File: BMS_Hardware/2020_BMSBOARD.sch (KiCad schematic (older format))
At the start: 145 parts

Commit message: schematic is done :)
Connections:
- net BUZZER: now also U?.PN2 (D1_8)
- net CELL_1-GND_SENSE: now also U?.PK3 (B2_8)
- net FAN_CTL_1: now also U?.PH2 (D1_3)
- net FAN_CTL_2: now also U?.PH3 (D1_4)
- net FAN_CTL_3: now also U?.PL5 (C1_6)
- net FAN_CTL_4: now also U?.PL4 (C1_5)
- net FAN_PWR: now also U?.PF1 (C1_1)
- net LOGIC_SWITCH: now also U?.PP2 (D1_10)
- net PACK_GATE: now also U?.PN3 (D1_9)
- net PACK_I_SENSE: now also U?.PE0 (B1_3)
- net SER_TX_IND: now also U?.PA5 (B2_10)
- net SW_IND: now also U?.PQ3 (D2_7)
- net TEMP_D_OUT: now also U?.PD1 (D1_6)
- net V_LOG_SENSE: now also U?.PE2 (B1_5)
- net V_OUT_SENSE: now also U?.PE1 (B1_4)
- net CELL8_SENSE: now reaches U?.PD4 (A2_5)
- net CELL7_SENSE: now reaches U?.PD5 (A2_6)
- net CELL6_SENSE: now reaches U?.PB4 (B2_3)
- net CELL5_SENSE: now reaches U?.PB5 (B2_4)
- net CELL4_SENSE: now reaches U?.PK0 (B2_5)
- net CELL3_SENSE: now reaches U?.PK1 (B2_6)
- net CELL2_SENSE: now reaches U?.PK2 (B2_7)
- net SW_EER: now reaches U?.PP3 (D2_8)
- no-connect marks 12 -> 53
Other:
- note added: "A1"
- note added: "A10"
- note added: "A11"
- note added: "A16"
- note added: "A17"
- note added: "A18"
- note added: "A19"
- note added: "A2"
- note added: "A3"
- note added: "A6\n"
- note added: "A7\n"
- moved on the sheet: B?, Conn?, Q?, R?

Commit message: fixed issues
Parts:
- gave numbers to parts that had none: 137
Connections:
- net GND: now also C9.2, D8.2 (A), D9.2 (A), R31.2
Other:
- moved on the sheet: C9, D8, D9, R29, R31

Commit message: schematic finished layout started
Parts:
- B1: footprint (none) -> MRDT_Devices:BUZZER_SMI_1324_TW_5V_2_R
- C1, C10, C11, C12, C13, C14, C15, C16, C17, C18, C19, C2, C20, C21, C3, C4, C5, C6, C7, C8, C9: footprint (none) -> Capacitor_SMD:C_0603_1608Metric_Pad1.05x0.95mm_HandSolder
- Conn1: footprint (none) -> MRDT_Connectors:Anderson_2_Vertical_Sidy_by_Side
- Conn10, Conn11: footprint (none) -> MRDT_Connectors:MOLEX_SL_09_Vertical
- Conn2, Conn5, Conn6, Conn7, Conn8: footprint (none) -> MRDT_Connectors:MOLEX_SL_02_Vertical
- Conn3, SW1: footprint (none) -> MRDT_Connectors:MOLEX_SL_04_Vertical
- Conn4, Conn9: footprint (none) -> MRDT_Connectors:MOLEX_SL_03_Vertical
- D1, D10, D11, D12, D13, D14, D15, D16, D2, D21, D23, D3, D4, D5, D6, D7, D8, D9: footprint (none) -> Diode_SMD:D_SOD-323_HandSoldering
- D17, D18, D19, D20, D22: footprint (none) -> LED_SMD:LED_0603_1608Metric_Pad1.05x0.95mm_HandSolder
- F1: footprint (none) -> Fuse:Fuse_0603_1608Metric_Pad1.05x0.95mm_HandSolder
- Q2, Q3: footprint (none) -> MRDT_Actives:IRLS3034_TO-263-7_P
- R1, R10, R11, R12, R13, R14, R15, R16, R17, R18, R19, R2, R20, R21, R22, R23, R24, R25, R26, R27, R28, R29, R3, R30, R31, R32, R33, R34, R35, R36, R37, R38, R39, R4, R40, R41, R42, R43, R44, R45, R46, R47, R48, R49, R5, R50, R51, R52, R53, R54, R55, R56, R6, R7, R8, R9: footprint (none) -> Resistor_SMD:R_0603_1608Metric_Pad1.05x0.95mm_HandSolder
- U1: footprint (none) -> Package_SO:SOIC-8-1EP_3.9x4.9mm_P1.27mm_EP2.29x3mm
- U10, U12: footprint (none) -> MRDT_Devices:OKI_Horizontal
- U11: footprint (none) -> MRDT_Shields:TM4C129E_Launchpad_FULL_SMD_TOP
- U2, U3, U4, U5, U6, U7, U8: footprint (none) -> Package_SO:SO-8_5.3x6.2mm_P1.27mm
- U9: footprint (none) -> MRDT_Sensors:ACS759ECB_PFF_Leadform_5pins
- V1, V2, V3: footprint (none) -> MRDT_Drill_Holes:BATT_PWR_VIA
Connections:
- net CELL_2_SENSE is gone; now on net CELL2_SENSE: D13.1 (K), R35.1
- net CELL_3_SENSE is gone; now on net CELL3_SENSE: D12.1 (K), R34.1
- net CELL_4_SENSE is gone; now on net CELL4_SENSE: D11.1 (K), R33.1
- net CELL_5_SENSE is gone; now on net CELL5_SENSE: D10.1 (K), R32.1
- net CELL_6_SENSE is gone; now on net CELL6_SENSE: D16.1 (K), R38.1
- net CELL_7_SENSE is gone; now on net CELL7_SENSE: D15.1 (K), R37.1
- net CELL_8_SENSE is gone; now on net CELL8_SENSE: D14.1 (K), R36.1

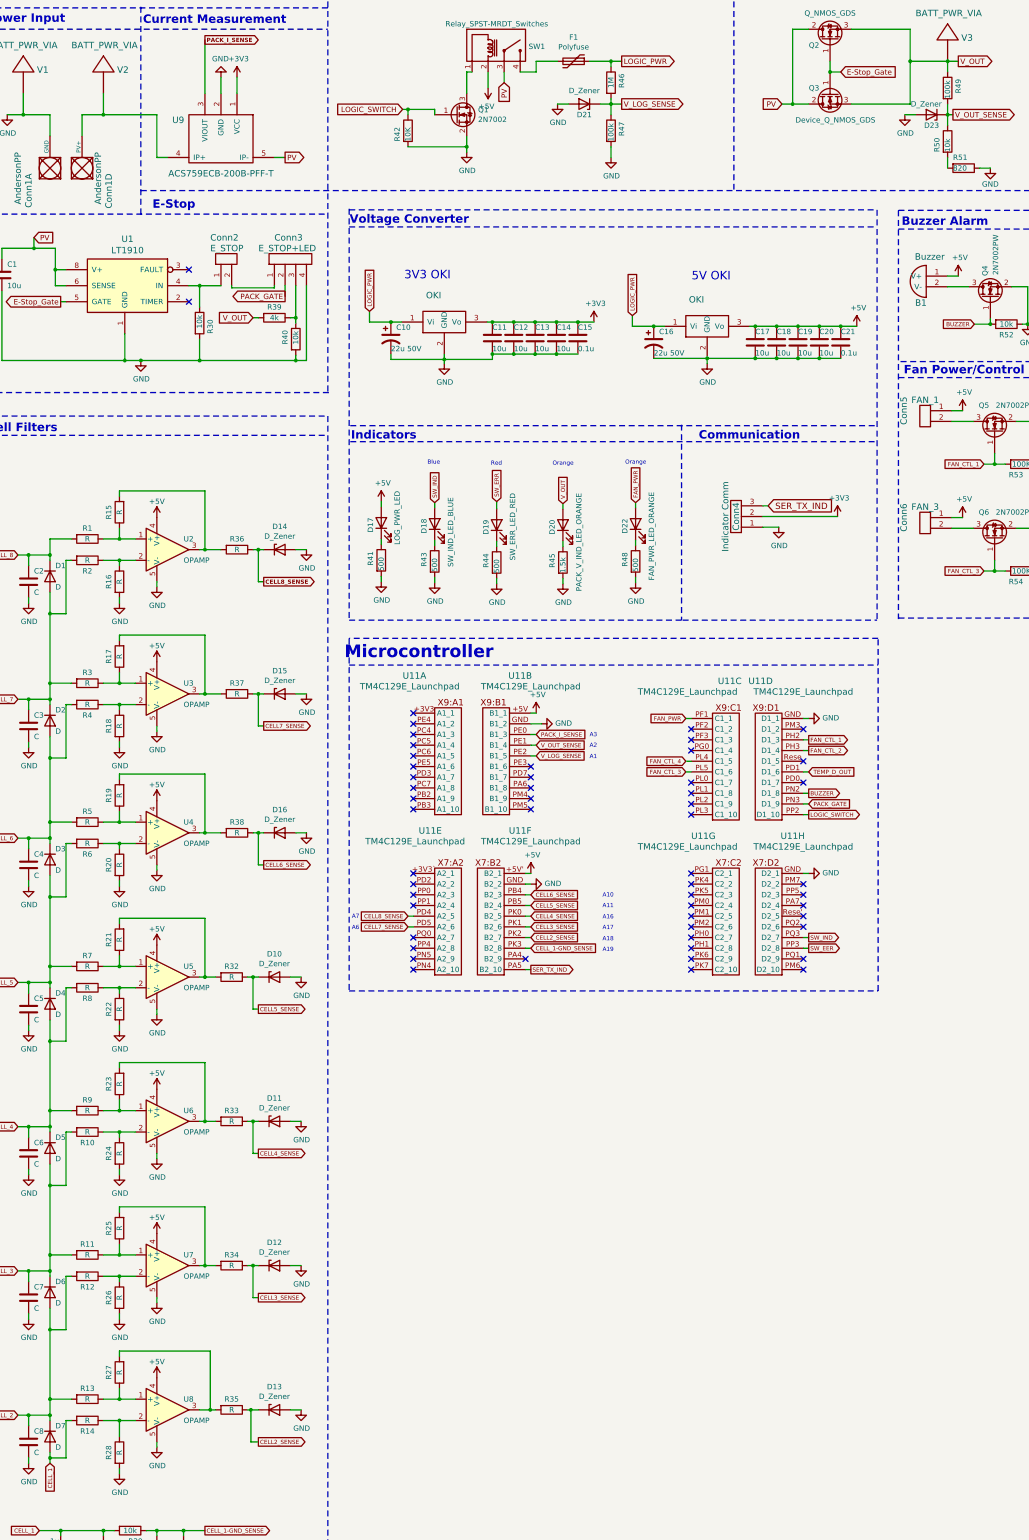
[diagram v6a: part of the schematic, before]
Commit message: updated layout
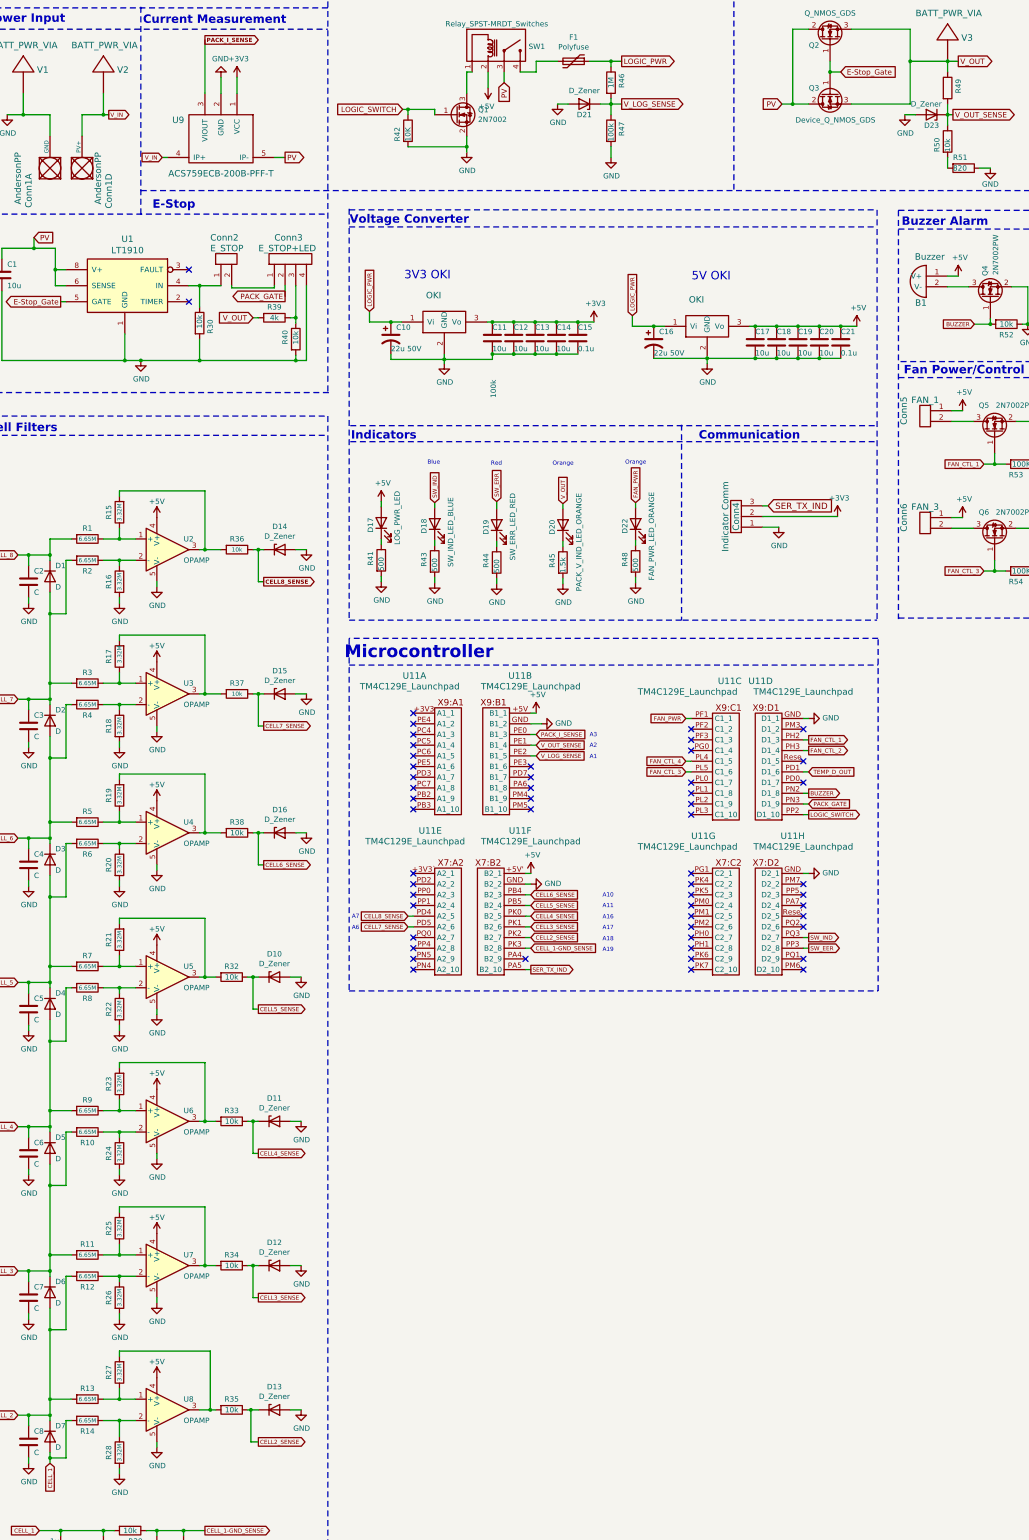
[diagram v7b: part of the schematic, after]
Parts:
- R1, R10, R11, R12, R13, R14, R2, R3, R4, R5, R6, R7, R8, R9: value R -> 6.65M
- R15, R16, R17, R18, R19, R20, R21, R22, R23, R24, R25, R26, R27, R28: value R -> 3.32M
- R32, R33, R34, R35, R36, R37, R38: value R -> 10k
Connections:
- net V_IN: now reaches Conn1.4 (PV+), U9.4 (IP+), V2.1

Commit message: Alisa, I pass the torch to you
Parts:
- B1: symbol MRDT_Devices:Buzzer -> 2020_BMSBOARD-rescue:Buzzer-MRDT_Devices
- Conn1: symbol MRDT_Connectors:AndersonPP -> 2020_BMSBOARD-rescue:AndersonPP-MRDT_Connectors
- Conn10, Conn11: symbol BMS_Hardware-rescue:Molex_SL_09-MRDT_Connectors -> 2020_BMSBOARD-rescue:Molex_SL_09-MRDT_Connectors-BMS_Hardware-rescue
- Conn2, Conn5, Conn6, Conn7, Conn8: symbol MRDT_Connectors:Molex_SL_02 -> 2020_BMSBOARD-rescue:Molex_SL_02-MRDT_Connectors
- Conn3: symbol BMS_Hardware-rescue:Molex_SL_04-MRDT_Connectors -> 2020_BMSBOARD-rescue:Molex_SL_04-MRDT_Connectors-BMS_Hardware-rescue
- Conn4: symbol BMS_Hardware-rescue:Molex_SL_03-MRDT_Connectors -> 2020_BMSBOARD-rescue:Molex_SL_03-MRDT_Connectors-BMS_Hardware-rescue
- Conn9: symbol MRDT_Connectors:Molex_SL_03 -> 2020_BMSBOARD-rescue:Molex_SL_03-MRDT_Connectors
- Q1, Q4, Q5, Q6, Q7, Q8: symbol BMS_Hardware-cache:2N7002 -> 2020_BMSBOARD-rescue:2N7002-BMS_Hardware-cache
- Q3: symbol BMS_Hardware-cache:Device_Q_NMOS_GDS -> 2020_BMSBOARD-rescue:Device_Q_NMOS_GDS-BMS_Hardware-cache
- SW1: symbol BMS_Hardware-rescue:Relay_SPST-MRDT_Switches -> 2020_BMSBOARD-rescue:Relay_SPST-MRDT_Switches-BMS_Hardware-rescue
- U1: symbol MRDT_ICs:LT1910 -> 2020_BMSBOARD-rescue:LT1910-MRDT_ICs
- U10, U12: symbol MRDT_Devices:OKI -> 2020_BMSBOARD-rescue:OKI-MRDT_Devices
- U11: symbol MRDT_Shields:TM4C129E_Launchpad -> 2020_BMSBOARD-rescue:TM4C129E_Launchpad-MRDT_Shields
- U9: symbol MRDT_Sensors:ACS759ECB-200B-PFF-T -> 2020_BMSBOARD-rescue:ACS759ECB-200B-PFF-T-MRDT_Sensors
- V1, V2, V3: symbol MRDT_Drill_Holes:BATT_PWR_VIA -> 2020_BMSBOARD-rescue:BATT_PWR_VIA-MRDT_Drill_Holes
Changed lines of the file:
@@
 $EndDescr
 $Comp
-L MRDT_Drill_Holes:BATT_PWR_VIA V1
+L 2020_BMSBOARD-rescue:BATT_PWR_VIA-MRDT_Drill_Holes V1
 U 1 1 5D928091
 P 850 1400
@@
 $EndComp
 $Comp
-L MRDT_Drill_Holes:BATT_PWR_VIA V2
+L 2020_BMSBOARD-rescue:BATT_PWR_VIA-MRDT_Drill_Holes V2
 U 1 1 5D928D3D
 P 1600 1400
@@
 $EndComp
 $Comp
-L MRDT_Connectors:AndersonPP Conn1
+L 2020_BMSBOARD-rescue:AndersonPP-MRDT_Connectors Conn1
 U 1 1 5D9296C4
 P 1200 2400
@@
 $EndComp
 $Comp
-L MRDT_Connectors:Molex_SL_02 Conn2
+L 2020_BMSBOARD-rescue:Molex_SL_02-MRDT_Connectors Conn2
 U 1 1 5D9A7186
 P 2850 3200
@@
 $EndComp
 $Comp
-L BMS_Hardware-rescue:Molex_SL_04-MRDT_Connectors Conn3
+L 2020_BMSBOARD-rescue:Molex_SL_04-MRDT_Connectors-BMS_Hardware-rescue Conn3
 U 1 1 5D9AC271
 P 3550 3200
@@
 E-Stop_Gate
 $Comp
-L MRDT_ICs:LT1910 U1
+L 2020_BMSBOARD-rescue:LT1910-MRDT_ICs U1
 U 1 1 5D996D94
 P 2200 3650
@@
 	3700 800  450  800
 $Comp
-L MRDT_Drill_Holes:BATT_PWR_VIA V3
+L 2020_BMSBOARD-rescue:BATT_PWR_VIA-MRDT_Drill_Holes V3
 U 1 1 5D988895
 P 9500 1100
@@
 	8050 1000 8050 1700
 $Comp
-L BMS_Hardware-cache:Device_Q_NMOS_GDS Q3
+L 2020_BMSBOARD-rescue:Device_Q_NMOS_GDS-BMS_Hardware-cache Q3
 U 1 1 5D980165
 P 8400 1600
@@
 Logic Power Switch
 $Comp
-L BMS_Hardware-rescue:Relay_SPST-MRDT_Switches SW1
+L 2020_BMSBOARD-rescue:Relay_SPST-MRDT_Switches-BMS_Hardware-rescue SW1
 U 1 1 5D928D53
 P 5000 1300
@@
 	4450 1750 4700 1750
 $Comp
-L BMS_Hardware-cache:2N7002 Q1
+L 2020_BMSBOARD-rescue:2N7002-BMS_Hardware-cache Q1
 U 1 1 5D9309B8
 P 4900 1800
@@
 	6550 3780 6750 3780
 $Comp
-L MRDT_Devices:OKI U12
+L 2020_BMSBOARD-rescue:OKI-MRDT_Devices U12
 U 1 1 5DA97369
 P 7050 3880
@@
 Voltage Monitoring
 $Comp
-L MRDT_Devices:Buzzer B1
+L 2020_BMSBOARD-rescue:Buzzer-MRDT_Devices B1
 U 1 1 5E2F5F41
 P 9300 3510
@@
 $EndComp
 $Comp
-L BMS_Hardware-cache:2N7002 Q4
+L 2020_BMSBOARD-rescue:2N7002-BMS_Hardware-cache Q4
 U 1 1 5E2FEEF8
 P 9900 3510
@@
 Connection ~ 10250 3760
 $Comp
-L MRDT_Connectors:Molex_SL_03 Conn9
+L 2020_BMSBOARD-rescue:Molex_SL_03-MRDT_Connectors Conn9
 U 1 1 5E338BAA
 P 11440 3600
@@
 	9040 2870 14890 2870
 $Comp
-L BMS_Hardware-rescue:Molex_SL_09-MRDT_Connectors Conn11
+L 2020_BMSBOARD-rescue:Molex_SL_09-MRDT_Connectors-BMS_Hardware-rescue Conn11
 U 1 1 5E1D4E30
 P 14130 3880
@@
 	9060 4110 14890 4110
 $Comp
-L BMS_Hardware-rescue:Molex_SL_09-MRDT_Connectors Conn10
+L 2020_BMSBOARD-rescue:Molex_SL_09-MRDT_Connectors-BMS_Hardware-rescue Conn10
 U 1 1 5E1D38F6
 P 12940 3880
@@
 	9040 4260 12410 4260
 $Comp
-L MRDT_Connectors:Molex_SL_02 Conn5
+L 2020_BMSBOARD-rescue:Molex_SL_02-MRDT_Connectors Conn5
 U 1 1 5E62A932
 P 9340 4720
@@
 	9540 4570 9640 4570
 $Comp
-L BMS_Hardware-cache:2N7002 Q5
+L 2020_BMSBOARD-rescue:2N7002-BMS_Hardware-cache Q5
 U 1 1 5E634A27
 P 9940 4770
@@
 $EndComp
 $Comp
-L MRDT_Connectors:Molex_SL_02 Conn7
+L 2020_BMSBOARD-rescue:Molex_SL_02-MRDT_Connectors Conn7
 U 1 1 5E66B9F8
 P 10990 4720
@@
 	11190 4570 11290 4570
 $Comp
-L BMS_Hardware-cache:2N7002 Q7
+L 2020_BMSBOARD-rescue:2N7002-BMS_Hardware-cache Q7
 U 1 1 5E66BA05
 P 11590 4770
@@
 $EndComp
 $Comp
-L MRDT_Connectors:Molex_SL_02 Conn6
+L 2020_BMSBOARD-rescue:Molex_SL_02-MRDT_Connectors Conn6
 U 1 1 5E683A7C
 P 9340 5720
@@
 	9540 5570 9640 5570
 $Comp
-L BMS_Hardware-cache:2N7002 Q6
+L 2020_BMSBOARD-rescue:2N7002-BMS_Hardware-cache Q6
 U 1 1 5E683A89
 P 9940 5770
@@
 $EndComp
 $Comp
-L MRDT_Connectors:Molex_SL_02 Conn8
+L 2020_BMSBOARD-rescue:Molex_SL_02-MRDT_Connectors Conn8
 U 1 1 5E690119
 P 10990 5720
@@
 	11190 5570 11290 5570
 $Comp
-L BMS_Hardware-cache:2N7002 Q8
+L 2020_BMSBOARD-rescue:2N7002-BMS_Hardware-cache Q8
 U 1 1 5E690126
 P 11590 5770
@@
 	9040 2695 9040 6520
 $Comp
-L MRDT_Shields:TM4C129E_Launchpad U11
+L 2020_BMSBOARD-rescue:TM4C129E_Launchpad-MRDT_Shields U11
 U 1 1 5E8F22FE
 P 4700 8350
@@
 NoConn ~ 4500 8300
 $Comp
-L MRDT_Shields:TM4C129E_Launchpad U11
+L 2020_BMSBOARD-rescue:TM4C129E_Launchpad-MRDT_Shields U11
 U 2 1 5E96159F
 P 5400 8350
@@
 	2100 15400 2100 15450
 $Comp
-L MRDT_Connectors:AndersonPP Conn1
+L 2020_BMSBOARD-rescue:AndersonPP-MRDT_Connectors Conn1
 U 4 1 5EAA3DB1
 P 1500 2400
@@
 	5600 7500 5700 7500
 $Comp
-L MRDT_Shields:TM4C129E_Launchpad U11
+L 2020_BMSBOARD-rescue:TM4C129E_Launchpad-MRDT_Shields U11
 U 3 1 5EB413A1
 P 7300 8400
@@
 $EndComp
 $Comp
-L MRDT_Shields:TM4C129E_Launchpad U11
+L 2020_BMSBOARD-rescue:TM4C129E_Launchpad-MRDT_Shields U11
 U 4 1 5EB461DE
 P 7950 8400
@@
 	8200 7450 8150 7450
 $Comp
-L MRDT_Shields:TM4C129E_Launchpad U11
+L 2020_BMSBOARD-rescue:TM4C129E_Launchpad-MRDT_Shields U11
 U 5 1 5EB5C834
 P 4700 9850
@@
 $EndComp
 $Comp
-L MRDT_Shields:TM4C129E_Launchpad U11
+L 2020_BMSBOARD-rescue:TM4C129E_Launchpad-MRDT_Shields U11
 U 6 1 5EB607C5
 P 5350 9850
@@
 $EndComp
 $Comp
-L MRDT_Shields:TM4C129E_Launchpad U11
+L 2020_BMSBOARD-rescue:TM4C129E_Launchpad-MRDT_Shields U11
 U 7 1 5EB94AA4
 P 7300 9850
@@
 	5600 9000 5550 9000
 $Comp
-L MRDT_Shields:TM4C129E_Launchpad U11
+L 2020_BMSBOARD-rescue:TM4C129E_Launchpad-MRDT_Shields U11
 U 8 1 5EBD95E0
 P 7950 9850
@@
 	7010 6530 3900 6530
 $Comp
-L BMS_Hardware-rescue:Molex_SL_03-MRDT_Connectors Conn4
+L 2020_BMSBOARD-rescue:Molex_SL_03-MRDT_Connectors-BMS_Hardware-rescue Conn4
 U 1 1 5DAE28B0
 P 7570 5410
@@
 $EndComp
 $Comp
-L MRDT_Devices:OKI U10
+L 2020_BMSBOARD-rescue:OKI-MRDT_Devices U10
 U 1 1 5DA4663D
 P 4590 3840
@@
 	3300 2200 3200 2200
 $Comp
-L MRDT_Sensors:ACS759ECB-200B-PFF-T U9
+L 2020_BMSBOARD-rescue:ACS759ECB-200B-PFF-T-MRDT_Sensors U9
 U 1 1 5D93BB0E
 P 3000 1800
